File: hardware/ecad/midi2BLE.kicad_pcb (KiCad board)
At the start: 4 copper layers, 75 x 40 mm, 64 parts, among them J1 USB_C_Receptacle, J2 Conn_01x02, J4 Conn_01x07, J6 Conn_01x04, SW1 SW_Push, SW2 SW_Push, SW3 SW_SPDT, U1 BQ24079RGTT, U2 TPS62162DSG, U3 TLV61047DDC, U4 ESP32-S3-WROOM-1, U5 TPS2116DRL, U6 TS3USB30EDGSR

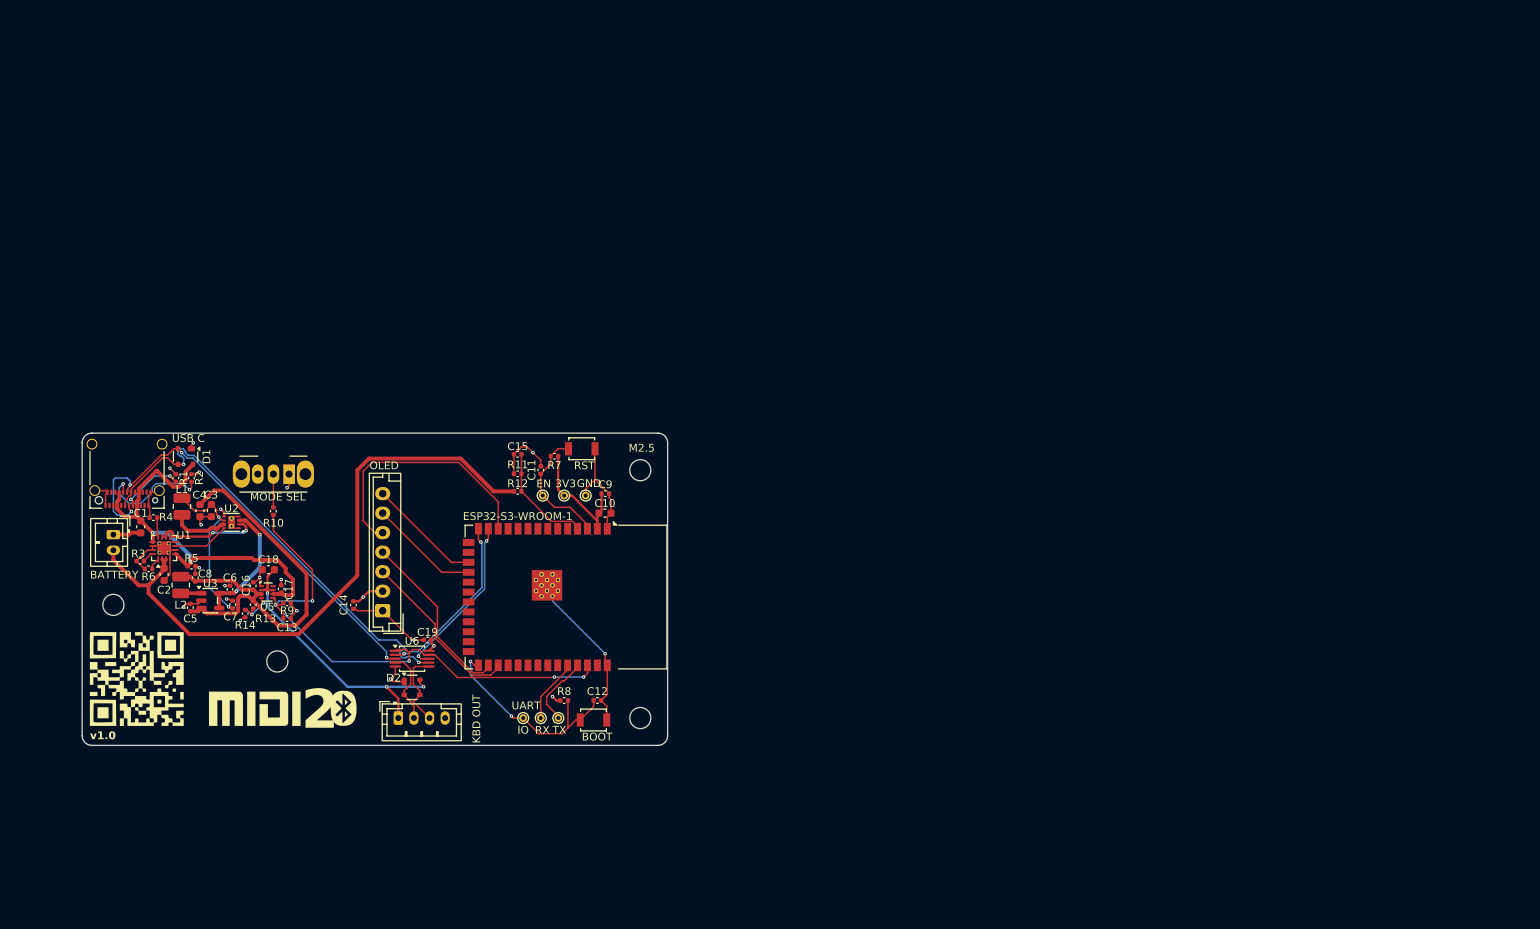
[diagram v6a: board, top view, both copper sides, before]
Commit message: Fixed minor errors and smaller issues withing schematics, moved v1 pcb and specific projet artifacts to archive. Produced PDF of full schematic
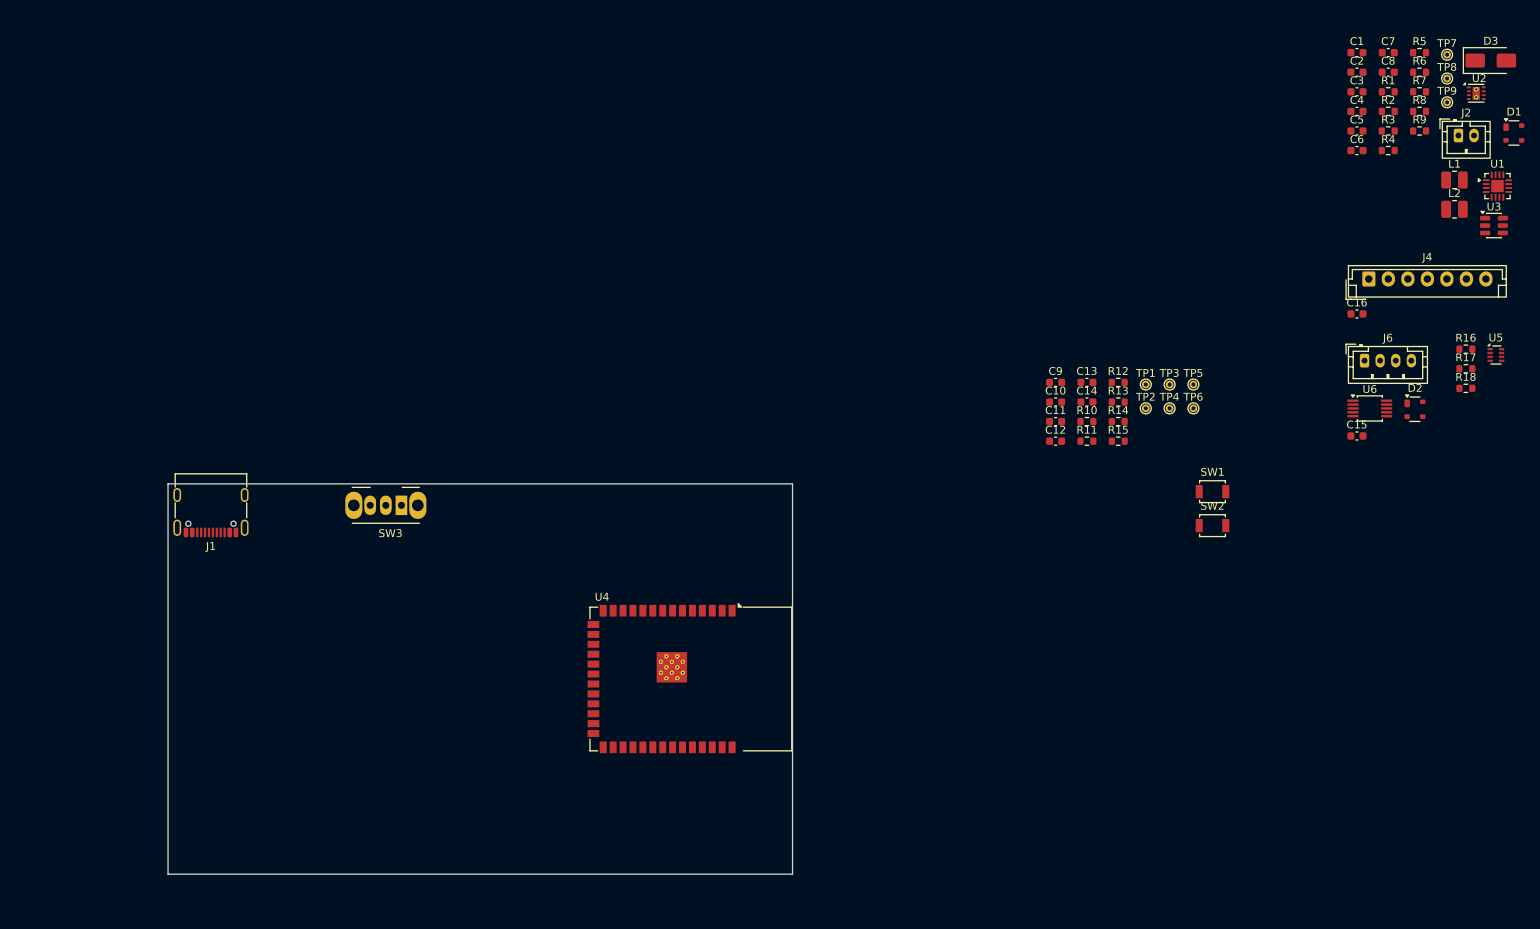
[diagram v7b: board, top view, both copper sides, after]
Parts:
- removed C17, C19: 100nF, Capacitor_SMD:C_0402_1005Metric
- removed C18: 10uF, Capacitor_SMD:C_0603_1608Metric
- removed G*** (x4): LOGO, LOGO
- removed REF** (x4): MountingHole_2.7mm_M2.5, MountingHole:MountingHole_2.7mm_M2.5
- added D3: SS14, Diode_SMD:D_SMA, F.Cu at (279.4, 20.8)
- added R15: 10k, Resistor_SMD:R_0603_1608Metric, F.Cu at (231.7, 69.5)
- added R16: 100k, Resistor_SMD:R_0603_1608Metric, F.Cu at (276.3, 57.7)
- added R17: 27k, Resistor_SMD:R_0603_1608Metric, F.Cu at (276.3, 60.3)
- added R18: 100k, Resistor_SMD:R_0603_1608Metric, F.Cu at (276.3, 62.8)
- added TP7: TestPoint, TestPoint:TestPoint_THTPad_D1.0mm_Drill0.5mm, F.Cu at (273.9, 20.0)
- added TP8: TestPoint, TestPoint:TestPoint_THTPad_D1.0mm_Drill0.5mm, F.Cu at (273.9, 23.1)
- added TP9: TestPoint, TestPoint:TestPoint_THTPad_D1.0mm_Drill0.5mm, F.Cu at (273.9, 26.1)
- C10: value 10uF -> 100nF
- C11, C13, C14, C15, C16, C5, C6, C9: footprint Capacitor_SMD:C_0402_1005Metric -> Capacitor_SMD:C_0603_1608Metric
- C12, C7: value 100nF -> 10uF; footprint Capacitor_SMD:C_0402_1005Metric -> Capacitor_SMD:C_0603_1608Metric
- C8: value 100nF -> 22uF; footprint Capacitor_SMD:C_0402_1005Metric -> Capacitor_SMD:C_0603_1608Metric
- J1: value USB_C_Receptacle -> USB_C_Receptacle_USB2.0_14P; footprint Connector_USB:USB_C_Receptacle_Amphenol_12401610E4-2A_CircularHoles -> Connector_USB:USB_C_Receptacle_G-Switch_GT-USB-7010ASV
- L2: value 2.2uH -> 4.7uH
- R1, R12, R2, R4, R5, R6: footprint Capacitor_SMD:C_0402_1005Metric -> Resistor_SMD:R_0603_1608Metric
- R10: value 100 -> 10k; footprint Capacitor_SMD:C_0402_1005Metric -> Resistor_SMD:R_0603_1608Metric
- R11: value 220k -> 100; footprint Capacitor_SMD:C_0402_1005Metric -> Resistor_SMD:R_0603_1608Metric
- R13: value 100k -> 220k; footprint Capacitor_SMD:C_0402_1005Metric -> Resistor_SMD:R_0603_1608Metric
- R14: value 100k -> 10k; footprint Capacitor_SMD:C_0402_1005Metric -> Resistor_SMD:R_0603_1608Metric
- R3: value 590 -> 680; footprint Capacitor_SMD:C_0402_1005Metric -> Resistor_SMD:R_0603_1608Metric
- R7: value 10k -> 180k; footprint Capacitor_SMD:C_0402_1005Metric -> Resistor_SMD:R_0603_1608Metric
- R8: value 10k -> 51k; footprint Capacitor_SMD:C_0402_1005Metric -> Resistor_SMD:R_0603_1608Metric
- R9: value 10k -> 100k; footprint Capacitor_SMD:C_0402_1005Metric -> Resistor_SMD:R_0603_1608Metric
- U1: value BQ24079RGTT -> BQ24075RGT; footprint Package_DFN_QFN:VQFN-16-1EP_3x3mm_P0.5mm_EP1.68x1.68mm_ThermalVias -> Package_DFN_QFN:VQFN-16-1EP_3x3mm_P0.5mm_EP1.6x1.6mm
- U3: value TLV61047DDC -> MT3608; footprint Package_TO_SOT_SMD:SOT-23-5 -> Package_TO_SOT_SMD:SOT-23-6
- moved J2 179.7 mm to (275.3, 30.4), turned to 0 degrees
- moved U1 177.0 mm to (280.3, 36.9), turned to 0 degrees
- moved D1 175.1 mm to (282.4, 30.1), turned to 0 degrees
- moved R6 174.8 mm to (270.3, 22.3)
- moved U3 171.3 mm to (279.9, 41.9)
- moved R5 170.5 mm to (270.3, 19.8), turned to 0 degrees
- moved L2 170.1 mm to (274.8, 39.8), turned to 0 degrees
- moved R3 169.1 mm to (266.3, 29.8)
- moved U2 168.7 mm to (277.6, 25.0), turned to 0 degrees
- moved L1 168.3 mm to (274.8, 36.1), turned to 0 degrees
- moved C1 167.2 mm to (262.3, 19.8), turned to 0 degrees
- moved C8 166.0 mm to (266.3, 22.3), turned to 0 degrees
- moved C2 165.8 mm to (262.3, 22.3), turned to 0 degrees
- moved R4 165.0 mm to (266.3, 32.3)
- moved C7 164.1 mm to (266.3, 19.8), turned to 0 degrees
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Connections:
- net /Power/J1 CC1 - R1 P1 renamed Net-(J1-CC1)
- net /Power/J1 CC2 - R2 P1 renamed Net-(J1-CC2)
- net /Power/U1 TS - R6 P1 renamed Net-(U1-TS)
- net /Power/U2 SW - L1 P1 renamed Net-(U2-SW)
- C10 pad 1: SYS_3V3 -> /ESP32_S3/BAT_SENSE
- C11 pad 1: /ESP32_S3/RST_BUTTON -> SYS_3V3
- C12 pad 1: /ESP32_S3/BOOT_BUTTON -> SYS_3V3
- C13 pad 1: GND -> /ESP32_S3/RST_BUTTON
- C13 pad 2: MODE_SEL -> GND
- C14 pad 1: SYS_3V3 -> /ESP32_S3/BOOT_BUTTON
- C15 pad 1: BAT_SENSE -> GND
- C15 pad 2: GND -> SYS_3V3
- C16 pad 1: BOOST_5V -> SYS_3V3
- C3 pad 2: /Power/U2 FB - C3 P1 -> BOOST_5V
- C4 pad 2: BOOST_5V -> /Power/U1_OUT
- C6 pad 2: /Power/U2 EN - U3 VIN -> /Power/U1_OUT
- C7 pad 2: /Power/U2 FB - C3 P1 -> BOOST_5V
- C8 pad 1: GND -> SYS_3V3
- C8 pad 2: BOOST_5V -> GND
- C9 pad 1: SYS_3V3 -> GND
- C9 pad 2: GND -> MODE_SEL
- J1 pad A8: unconnected-(J1-SBU1-PadA8) -> (no net)
- J1 pad B8: unconnected-(J1-SBU2-PadB8) -> (no net)
- L1 pad 2: /Power/U2 FB - C3 P1 -> SYS_3V3
- L2 pad 1: Net-(U3-SW) -> /Power/U1_OUT
- L2 pad 2: BOOST_5V -> Net-(D3-A)
- R10 pad 2: Net-(SW3-B) -> GND
- R11 pad 1: GND -> MODE_SEL
- R11 pad 2: BAT_SENSE -> Net-(SW3-B)
- R12 pad 1: BAT_SENSE -> /ESP32_S3/BAT_SENSE
- R13 pad 1: Net-(U5-PR1) -> GND
- R13 pad 2: BOOST_5V -> /ESP32_S3/BAT_SENSE
- R14 pad 1: Net-(U5-PR1) -> SYS_3V3
- R14 pad 2: GND -> /ESP32_S3/RST_BUTTON
- R3 pad 1: GND -> Net-(U1-ISET)
- R3 pad 2: /Power/U1 ISET - R3 P1 -> GND
- R4 pad 1: GND -> Net-(U1-ILIM)
- R4 pad 2: /Power/U1 ILIM - R4 P1 -> GND
- R5 pad 1: GND -> SYS_3V3
- R5 pad 2: VBUS_IN -> /Power/U1_PGOOD
- R7 pad 1: SYS_3V3 -> Net-(U3-FB)
- R7 pad 2: /ESP32_S3/RST_BUTTON -> Net-(D3-A)
- R8 pad 1: SYS_3V3 -> GND
- R8 pad 2: /ESP32_S3/BOOT_BUTTON -> Net-(U3-FB)
- R9 pad 1: MODE_SEL -> /Power/U1_PGOOD
- R9 pad 2: GND -> SYS_3V3
- U1 pad 10: /Power/U1 OUT_2 - U2 VIN -> /Power/U1_OUT
- U1 pad 11: /Power/U1 OUT_2 - U2 VIN -> /Power/U1_OUT
- U1 pad 12: /Power/U1 ILIM - R4 P1 -> Net-(U1-ILIM)
- U1 pad 16: /Power/U1 ISET - R3 P1 -> Net-(U1-ISET)
- U1 pad 7: /Power/U2 PG - R7 P2 -> /Power/U1_PGOOD
- U2 pad 2: /Power/U1 OUT_2 - U2 VIN -> /Power/U1_OUT
- U2 pad 3: /Power/U2 EN - U3 VIN -> /Power/U1_OUT
- U2 pad 5: SYS_3V3 -> GND
- U2 pad 6: /Power/U2 FB - C3 P1 -> SYS_3V3
- U2 pad 8: /Power/U2 PG - R7 P2 -> /Power/U1_PGOOD
- U3 pad 1: Net-(U3-SW) -> Net-(D3-A)
- U3 pad 3: BOOST_5V -> Net-(U3-FB)
- U3 pad 4: /Power/U2 EN - U3 VIN -> /Power/U1_OUT
- U3 pad 5: /Power/U2 EN - U3 VIN -> /Power/U1_OUT
- U4 pad 31: unconnected-(U4-IO38-Pad31) -> USB_STATUS
- U4 pad 4: BAT_SENSE -> /ESP32_S3/RST_BUTTON
- U5 pad 3: BOOST_5V -> VBUS_IN
- U5 pad 5: MODE_SEL -> VBUS_IN
- U5 pad 6: VBUS_IN -> BOOST_5V
- U5 pad 8: unconnected-(U5-ST-Pad8) -> USB_STATUS
- U6 pad 9: MODE_SEL -> GND
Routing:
- net GND: track 100.8 -> 0.00 mm, vias 16 -> 0
- net BAT: track 81.5 -> 0.00 mm
- net MODE_SEL: track 72.3 -> 0.00 mm, vias 5 -> 0
- net USB_UP-: track 59.7 -> 0.00 mm, vias 2 -> 0
- net USB_UP+: track 59.0 -> 0.00 mm, vias 4 -> 0
- net BOOST_5V: track 56.4 -> 0.00 mm
- net VBUS_IN: track 52.7 -> 0.00 mm, vias 2 -> 0
- net VBUS_KBD: track 36.7 -> 0.00 mm, vias 3 -> 0
- net OLED_RES: track 32.8 -> 0.00 mm
- net /ESP32_S3/BOOT_BUTTON: track 27.6 -> 0.00 mm, vias 2 -> 0
- net SYS_3V3: track 27.0 -> 0.00 mm, vias 5 -> 0
- net USB_ESP+: track 23.3 -> 0.00 mm, vias 2 -> 0
- net OLED_MOSI: track 22.7 -> 0.00 mm
- net OLED_CLK: track 22.0 -> 0.00 mm
- net /Power/U2 FB - C3 P1: track 21.5 -> 0.00 mm, vias 2 -> 0
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- removed copper zone on In1.Cu, net GND
- removed copper zone on In2.Cu, net SYS_3V3
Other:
- board size 75 x 40 mm -> 80 x 50 mm
- board text removed: "2"
- board text removed: "3V3"
- board text removed: "BATTERY"
- board text removed: "BOOT"
- board text removed: "EN"
- board text removed: "ESP32-S3-WROOM-1"
- board text removed: "GND"
- board text removed: "IO"
- board text removed: "KBD OUT"
- board text removed: "M2.5"
- board text removed: "MODE SEL"
- board text removed: "OLED"
- board text removed: "RST"
- board text removed: "RX"
- board text removed: "TX"
- board text removed: "UART"
- board text removed: "USB C"
- board text removed: "nikhilsudhir 2026"
- board text removed: "v1.0"

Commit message: Fixed minor errors and smaller issues withing schematics, moved v1 pcb and specific projet artifacts to archive. Updated changelog and finsihed pcb fopr version 2
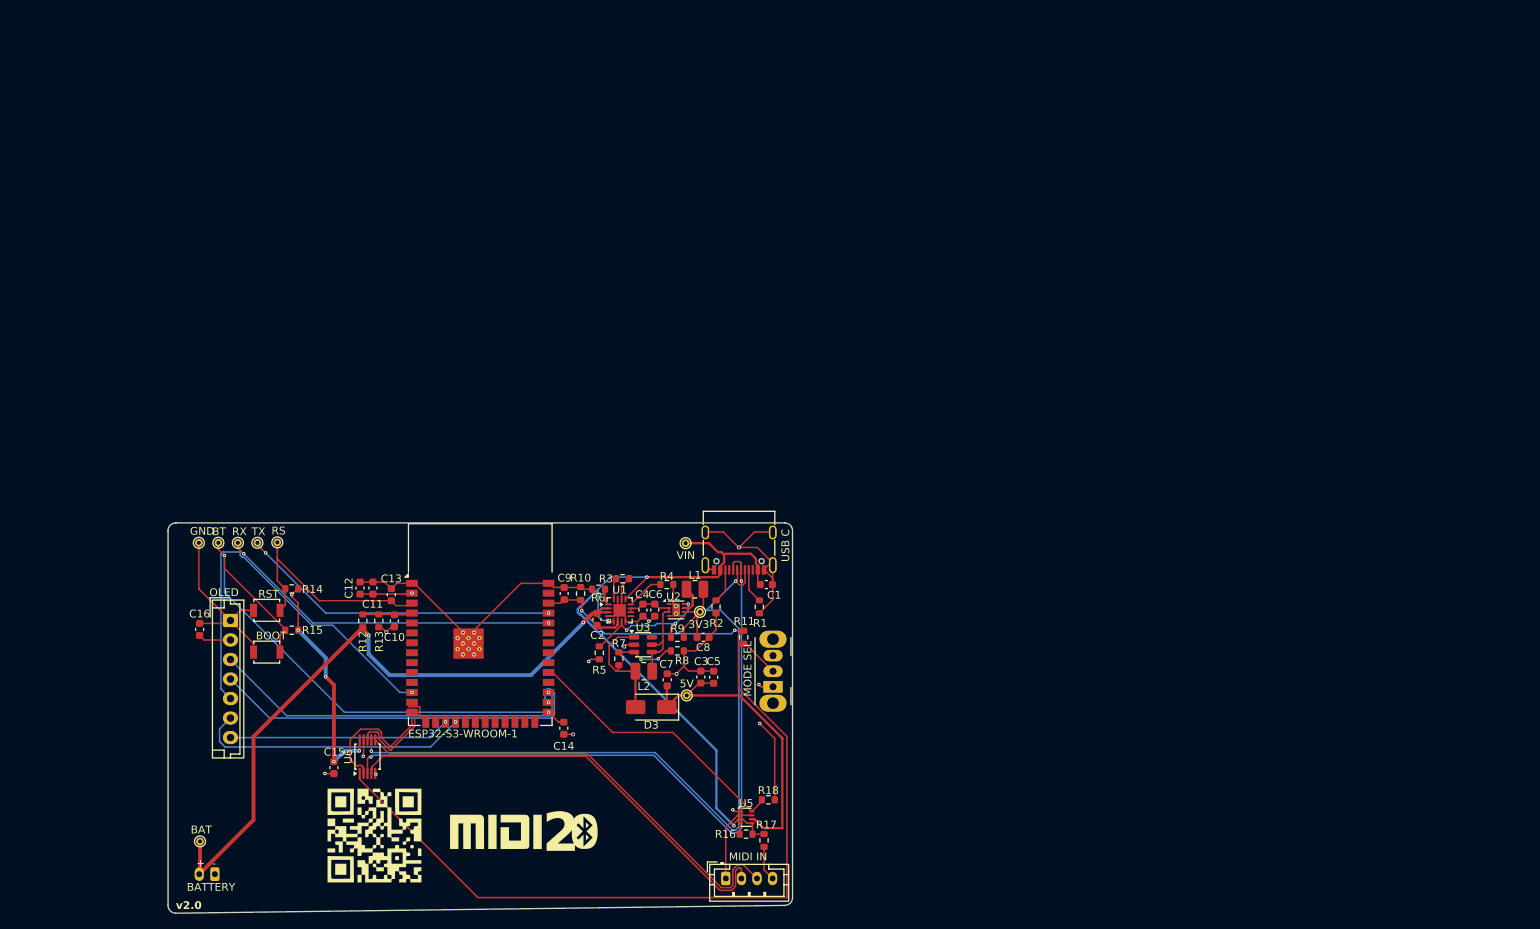
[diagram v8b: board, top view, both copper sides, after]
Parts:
- removed D1, D2: PRTR5V0U2X, Package_TO_SOT_SMD:SOT-143
- added G***: LOGO, LOGO, F.Cu at (152.1, 119.6)
- added G***: LOGO, LOGO, F.Cu at (136.4, 120.0)
- added G***: LOGO, LOGO, F.Cu at (163.4, 119.5)
- added G***: LOGO, LOGO, B.Cu at (145.5, 103.7)
- J2: moved to B.Cu
- moved TP9 185.7 mm to (114.1, 120.8)
- moved J2 185.3 mm to (116.0, 125.0), turned to 180 degrees
- moved C16 153.7 mm to (114.0, 93.7), turned to 90 degrees
- moved J4 152.2 mm to (118.0, 92.5), turned to -90 degrees
- moved C15 137.8 mm to (131.2, 111.3), turned to 90 degrees
- moved U6 135.9 mm to (135.6, 110.0), turned to 90 degrees
- moved D3 135.7 mm to (171.9, 103.6), turned to 180 degrees
- moved R5 130.2 mm to (165.2, 96.7), turned to 90 degrees
- moved TP6 126.1 mm to (116.5, 82.5)
- moved R7 125.7 mm to (167.8, 97.4), turned to -90 degrees
- moved TP8 125.4 mm to (176.4, 102.1)
- moved U1 124.9 mm to (167.8, 91.2)
- moved R6 124.3 mm to (165.2, 88.5)
- moved TP2 122.5 mm to (114.0, 82.5)
- moved C7 122.4 mm to (173.9, 100.1), turned to -90 degrees
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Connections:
- U4 pad 4: /ESP32_S3/RST_BUTTON -> /ESP32_S3/BAT_SENSE
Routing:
- net GND: track 0.00 -> 146.0 mm, vias 0 -> 10
- net SYS_3V3: track 0.00 -> 132.2 mm, vias 0 -> 9
- net MODE_SEL: track 0.00 -> 126.7 mm, vias 0 -> 2
- net USB_UP-: track 0.00 -> 93.5 mm, vias 0 -> 2
- net USB_UP+: track 0.00 -> 90.3 mm, vias 0 -> 2
- net VBUS_IN: track 0.00 -> 88.0 mm, vias 0 -> 3
- net BAT: track 0.00 -> 85.5 mm, vias 0 -> 2
- net /ESP32_S3/BOOT_BUTTON: track 0.00 -> 72.9 mm, vias 0 -> 2
- net USB_KBD-: track 0.00 -> 59.9 mm
- net USB_KBD+: track 0.00 -> 59.6 mm
- net OLED_RES: track 0.00 -> 51.3 mm, vias 0 -> 1
- net OLED_MOSI: track 0.00 -> 49.7 mm, vias 0 -> 1
- net OLED_CLK: track 0.00 -> 47.2 mm, vias 0 -> 1
- net /ESP32_S3/RX0: track 0.00 -> 44.5 mm, vias 0 -> 2
- net /ESP32_S3/TX0: track 0.00 -> 41.2 mm, vias 0 -> 2
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- added copper zone on In1.Cu, net GND
- added copper zone on In2.Cu, net SYS_3V3
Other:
- outline, holes or cut-outs redrawn
- board text added: "+"
- board text added: "-"
- board text added: "2"
- board text added: "3V3"
- board text added: "5V"
- board text added: "BAT"
- board text added: "BATTERY"
- board text added: "BOOT"
- board text added: "BT"
- board text added: "ESP32-S3-WROOM-1"
- board text added: "GND"
- board text added: "MIDI IN"
- board text added: "MODE SEL"
- board text added: "OLED"
- board text added: "RS"
- board text added: "RST"
- board text added: "RX"
- board text added: "TX"
- board text added: "USB C"
- board text added: "VIN"
- board text added: "v2.0"
